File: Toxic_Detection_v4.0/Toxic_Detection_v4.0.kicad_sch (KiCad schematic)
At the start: 14 parts, among them J2 Conn_ARM_JTAG_SWD_20, J3 USB_C_Receptacle, J4 Conn_01x04_Pin

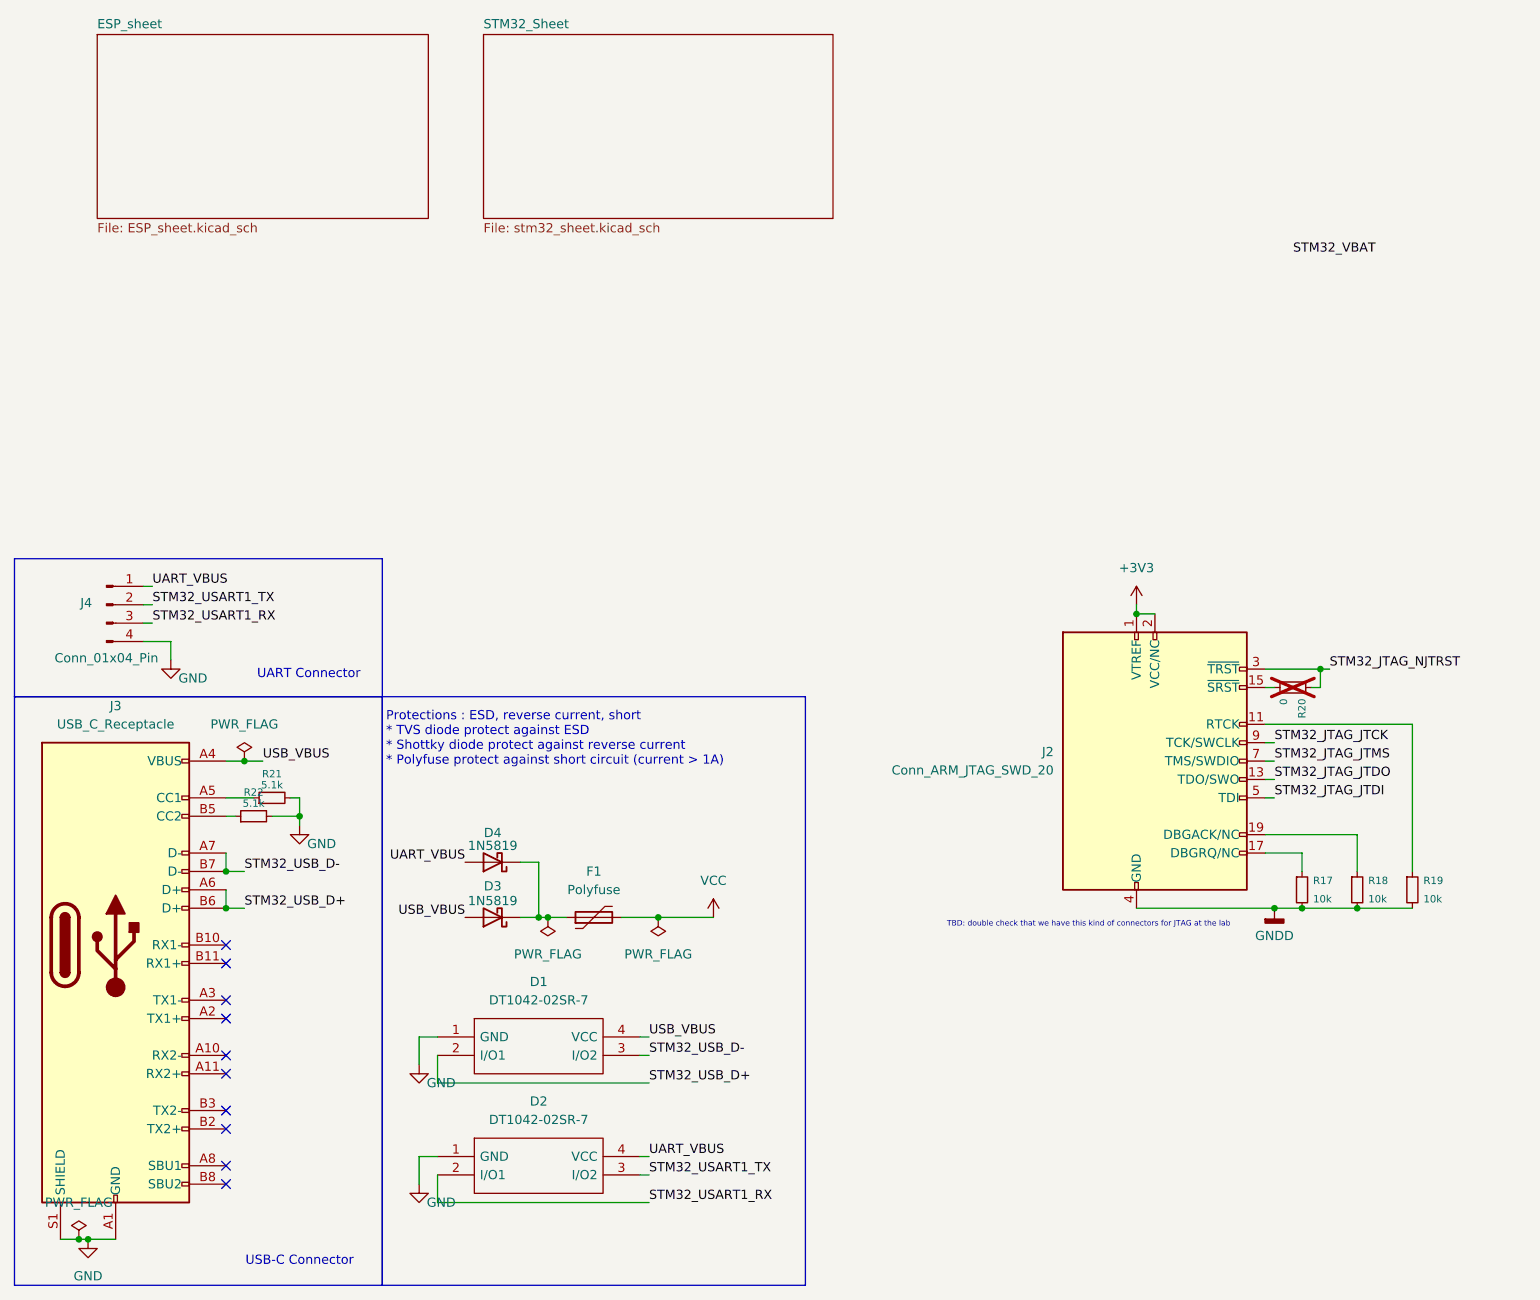
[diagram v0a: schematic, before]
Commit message: feat: add AFE connectors & ADCs. Add LDOs with power gating
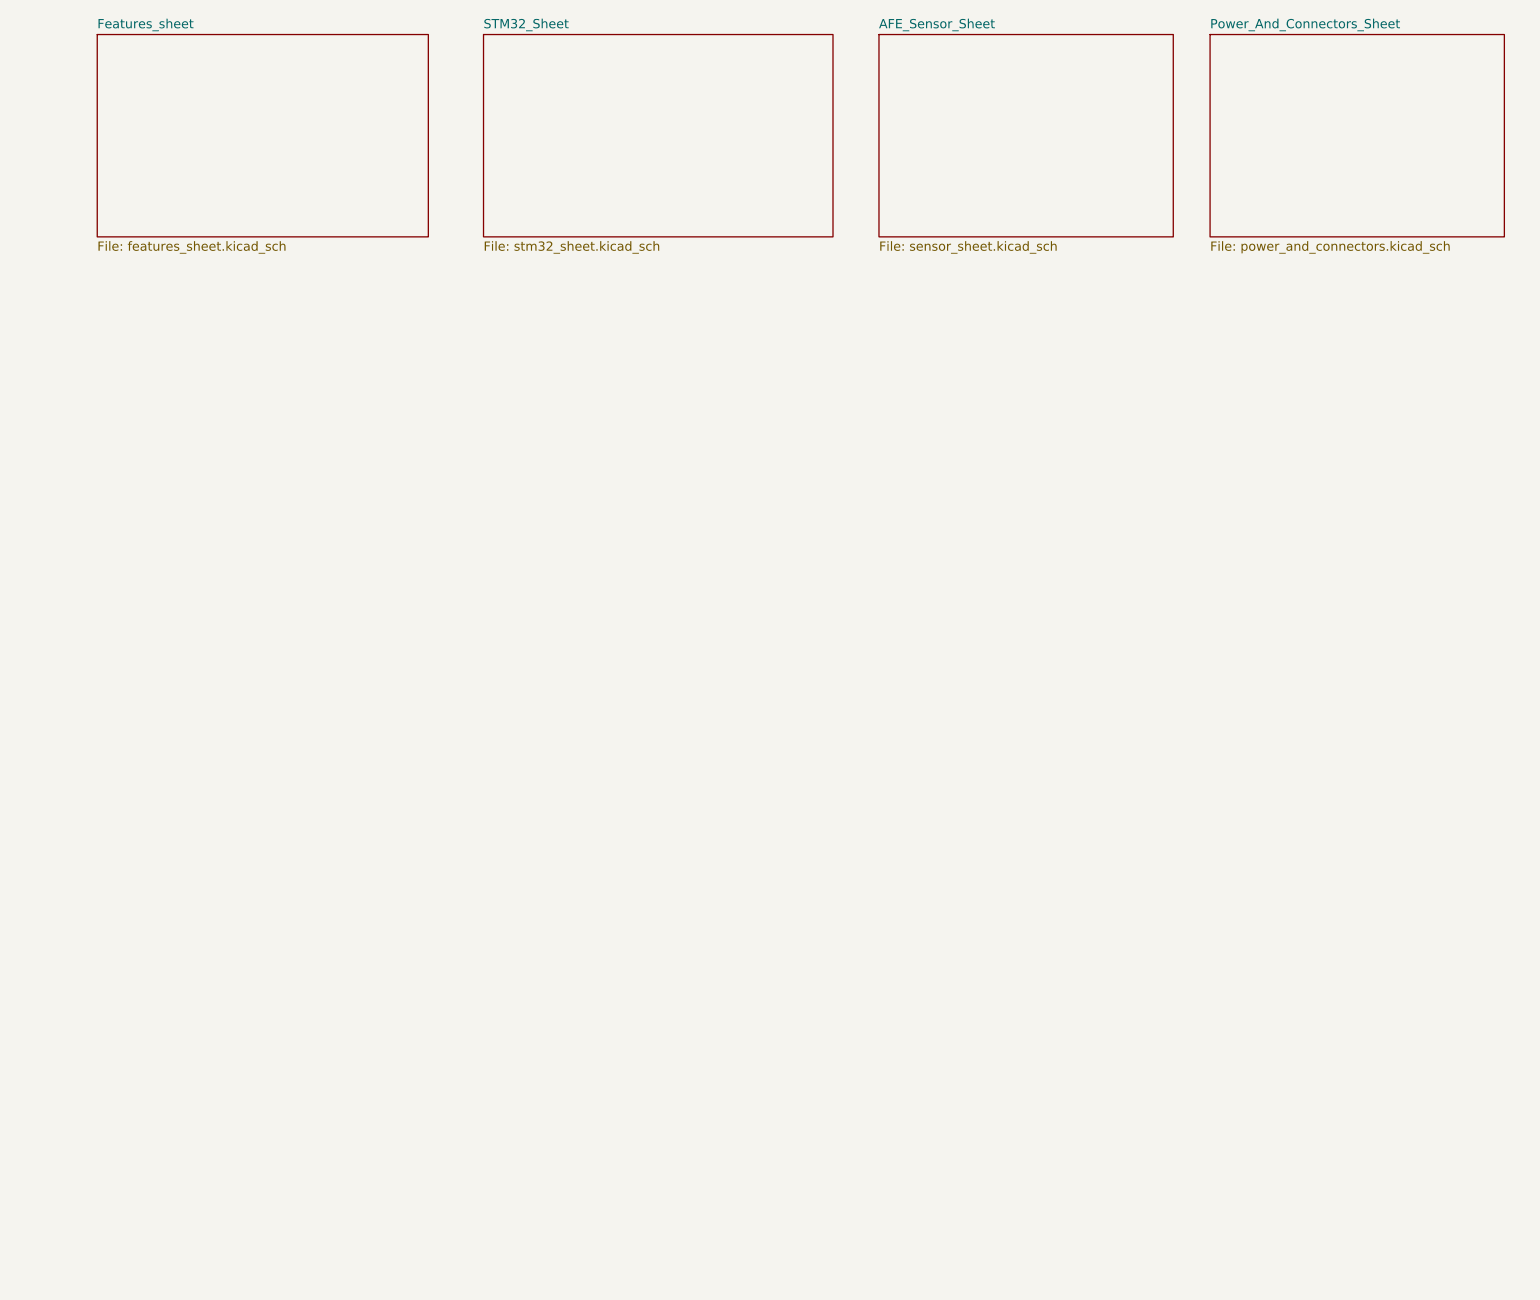
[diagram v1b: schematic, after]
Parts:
- removed D1, D2: DT1042-02SR-7, DT104202SR7, symbol DT1042-02SR-7:DT1042-02SR-7
- removed D3, D4: 1N5819, Diode_SMD:D_SOD-123, symbol Diode:1N5819
- removed F1: Polyfuse, Fuse:Fuse_1210_3225Metric_Pad1.42x2.65mm_HandSolder, symbol Device:Polyfuse
- removed J2: Conn_ARM_JTAG_SWD_20, symbol Connector:Conn_ARM_JTAG_SWD_20
- removed J3: USB_C_Receptacle, symbol Connector:USB_C_Receptacle
- removed J4: Conn_01x04_Pin, symbol Connector:Conn_01x04_Pin
- removed R17, R18, R19: 10k, symbol Device:R_Small
- removed R20: 0, symbol Device:R_Small
- removed R21, R22: 5.1k, symbol Device:R_Small
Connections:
- no-connect marks 10 -> 0
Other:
- sheet ESP_sheet renamed Features_sheet
- added sheet AFE_Sensor_Sheet (sensor_sheet.kicad_sch)
- added sheet Power_And_Connectors_Sheet (power_and_connectors.kicad_sch)
- sheet Features_sheet: file ESP_sheet.kicad_sch -> features_sheet.kicad_sch
- note removed: "Protections : ESD, reverse current, short * TVS diode protect against ESD * Shottky diode protect against reverse current * Polyfuse protect against short circuit (current > 1A)"
- note removed: "TBD: double check that we have this kind of connectors for JTAG at the lab"
- note removed: "UART Connector"
- note removed: "USB-C Connector"

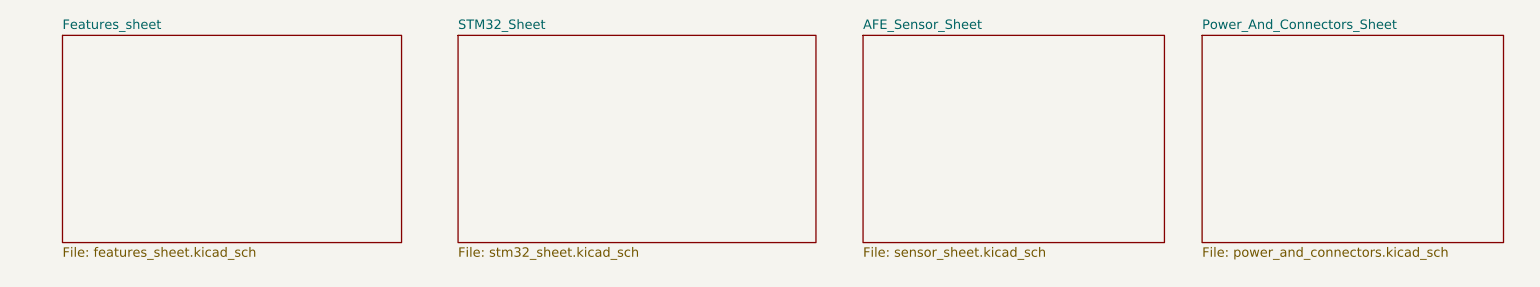
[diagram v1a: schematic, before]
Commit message: feat: add GNSS module and antenna
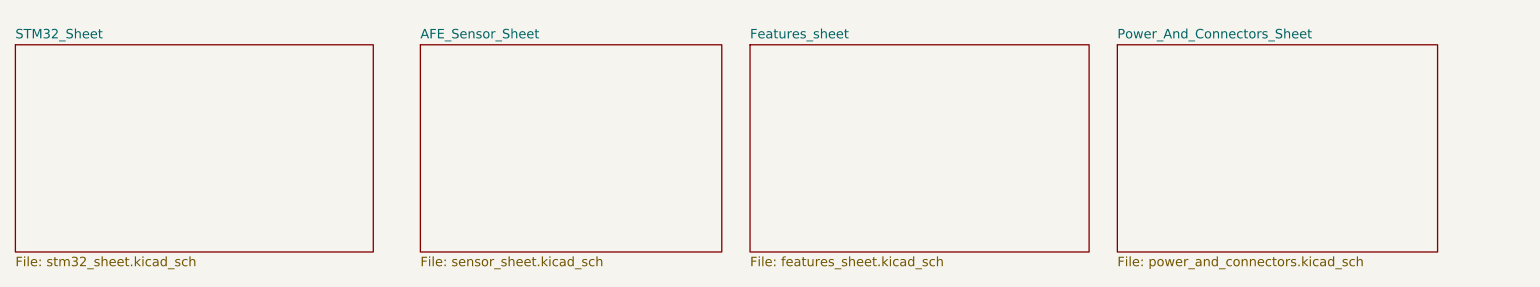
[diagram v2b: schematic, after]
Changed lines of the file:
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@@
 	)
 	(sheet
-		(at 132.08 24.13)
+		(at 72.39 25.4)
 		(size 40.64 27.94)
 		(exclude_from_sim no)
@@
 		)
 		(property "Sheetname" "AFE_Sensor_Sheet"
-			(at 132.08 23.4184 0)
+			(at 72.39 24.6884 0)
 			(effects
 				(font
@@
 		)
 		(property "Sheetfile" "sensor_sheet.kicad_sch"
-			(at 132.08 52.6546 0)
+			(at 72.39 53.9246 0)
 			(effects
 				(font
@@
 	)
 	(sheet
-		(at 77.47 24.13)
+		(at 17.78 25.4)
 		(size 48.26 27.94)
 		(exclude_from_sim no)
@@
 		)
 		(property "Sheetname" "STM32_Sheet"
-			(at 77.47 23.4184 0)
+			(at 17.78 24.6884 0)
 			(effects
 				(font
@@
 		)
 		(property "Sheetfile" "stm32_sheet.kicad_sch"
-			(at 77.47 52.6546 0)
+			(at 17.78 53.9246 0)
 			(effects
 				(font
@@
 	)
 	(sheet
-		(at 24.13 24.13)
+		(at 116.84 25.4)
 		(size 45.72 27.94)
 		(exclude_from_sim no)
@@
 		)
 		(property "Sheetname" "Features_sheet"
-			(at 24.13 23.4184 0)
+			(at 116.84 24.6884 0)
 			(effects
 				(font
@@
 		)
 		(property "Sheetfile" "features_sheet.kicad_sch"
-			(at 24.13 52.6546 0)
+			(at 116.84 53.9246 0)
 			(effects
 				(font
@@
 	)
 	(sheet
-		(at 177.8 24.13)
-		(size 40.64 27.94)
+		(at 166.37 25.4)
+		(size 43.18 27.94)
 		(exclude_from_sim no)
 		(in_bom yes)
@@
 		)
 		(property "Sheetname" "Power_And_Connectors_Sheet"
-			(at 177.8 23.4184 0)
+			(at 166.37 24.6884 0)
 			(effects
 				(font
@@
 		)
 		(property "Sheetfile" "power_and_connectors.kicad_sch"
-			(at 177.8 52.6546 0)
+			(at 166.37 53.9246 0)
 			(effects
 				(font
